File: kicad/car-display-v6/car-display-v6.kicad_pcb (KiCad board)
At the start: 4 copper layers, 35.8 x 35.8 mm, 38 parts, among them J1 AVR-ISP-10, J2 Screw_Terminal_01x03, J3 PicoBlade F 1x7, J4 Socket 1x6 0.1", J5 JMP 1x3 0.05", U1 ATmega328PB-M, U2 MCP25625T-E/ML, U3 TPSM365R1FRDNR, U4 TPSM365R15RDNR, Y1 16MHZ

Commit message: Work on V6 pCB
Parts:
- U3: value TPSM365R1FRDNR -> TPSM365R15FRDNR
- moved C17 0.13 mm to (96.5, 178.7)
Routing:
- net +12V: track 21.5 -> 4.43 mm, vias 0 -> 9
- net +3.3V: track 27.9 -> 30.2 mm
- net GND: vias 41 -> 49
- added copper zone on B.Cu, net +12V

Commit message: Work on V6 code for PlatformIO
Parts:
- removed the C1 at (91.2, 183.4)
- removed the C2 at (89.5, 182.8)
- removed the C3 at (83.4, 182.8)
- removed the C4 at (86.6, 177.8)
- added FB3: 120X, Inductor_SMD:L_0402_1005Metric, F.Cu at (91.2, 163.3)
- added FB4: 120X, Inductor_SMD:L_0402_1005Metric, F.Cu at (89.8, 163.3)
- added FB5: 120X, Inductor_SMD:L_0402_1005Metric, F.Cu at (88.4, 163.3)
- added FB6: 120X, Inductor_SMD:L_0402_1005Metric, F.Cu at (87.0, 163.3)
- added FB7: 120X, Inductor_SMD:L_0402_1005Metric, F.Cu at (85.6, 163.3)
- added H3: MountingHole_Pad, MountingHole:MountingHole_2.2mm_M2_DIN965, F.Cu at (84.5, 173.1)
- C1: renamed from C17; value C_Polarized -> 100uF
- FB1, FB2: value FerriteBead_Small_Array -> 120X; footprint jsdev:fb_array_0805 -> Inductor_SMD:L_0402_1005Metric
- U2: value MCP25625T-E/ML -> MCP2515-xST; footprint jsdev:QFN-28-1EP_6x6mm_P0.65mm_EP4.25x4.25mm_mod1 -> Package_SO:TSSOP-20_4.4x6.5mm_P0.65mm
- U3: value TPSM365R15FRDNR -> TCAN332; footprint jsdev:QFN-FCMOD_TI_11B -> jsdev:SOT-23-8-MOD
- moved H2 21.6 mm to (84.5, 187.1)
- moved U3 20.1 mm to (106.4, 178.6), turned to 0 degrees
- moved J4 16.2 mm to (115.6, 161.5), turned to 0 degrees
- moved J5 15.6 mm to (109.8, 173.0), turned to 180 degrees
- moved H1 15.2 mm to (114.9, 156.6)
- moved R4 14.8 mm to (111.9, 174.1), turned to 90 degrees
- moved R3 14.4 mm to (97.3, 172.7)
- moved C12 9.98 mm to (104.9, 167.4), turned to 180 degrees
- moved C3 9.78 mm to (91.2, 182.8)
- moved C4 9.78 mm to (89.5, 182.1)
- moved C5 9.78 mm to (83.4, 182.1)
- moved C6 9.78 mm to (86.6, 177.2)
- moved U4 9.78 mm to (86.6, 181.1)
- moved J1 9.09 mm to (87.2, 169.3)
- moved C2 8.30 mm to (111.0, 167.3), turned to -90 degrees
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- renumbered C13 to C10, C14 to C11, C15 to C12, C16 to C13, C9 to C2, C5 to C3, C6 to C4, C7 to C5, C8 to C6, C10 to C7, C11 to C8, C12 to C9, R6 to R1, R5 to R2, R8 to R3, R7 to R4
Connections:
- C13 pad 1: +5V -> +3.3V
- FB1 pad 2: /3F_SCK -> MOSI
- FB2 pad 1: /3F_CS_OLED -> /3F_SCK
- FB2 pad 2: /3F_GND -> SCK
- U1 pad 11: INT_CAN -> unconnected-(U1-PD7-Pad11)
- U1 pad 25: SEL_UNIT -> INT_CAN
- U1 pad 26: unconnected-(U1-PC3-Pad26) -> SEL_UNIT
- U2 pad 1: CS_CAN -> T_{X}CAN
- U2 pad 10: R_{X}CAN -> GND
- U2 pad 11: +3.3V -> unconnected-(U2-~{RX1BF}-Pad11)
- U2 pad 12: GND -> unconnected-(U2-~{RX0BF}-Pad12)
- U2 pad 13: CANH -> INT_CAN
- U2 pad 14: unconnected-(U2-NC-Pad14) -> SCK
- U2 pad 15: GND -> unconnected-(U2-NC-Pad15)
- U2 pad 16: T_{X}CAN -> MOSI
- U2 pad 17: unconnected-(U2-NC-Pad17) -> MISO
- U2 pad 18: GND -> CS_CAN
- U2 pad 19: +5V -> RESET
- U2 pad 2: RESET -> R_{X}CAN
- U2 pad 20: /CAN_CLK_PD -> +3.3V
- U2 pad 3: +3.3V -> unconnected-(U2-CLKOUT/SOF-Pad3)
- U2 pad 4: T_{X}CAN -> unconnected-(U2-~{TX0RTS}-Pad4)
- U2 pad 5: R_{X}CAN -> unconnected-(U2-~{TX1RTS}-Pad5)
- U2 pad 8: unconnected-(U2-~{TX1RTS}-Pad8) -> /CAN_CLK_PD
- U2 pad 9: unconnected-(U2-~{TX2RTS}-Pad9) -> CLK
- U3 pad 1: unconnected-(U3-PGOOD-Pad1) -> T_{X}CAN
- U3 pad 2: unconnected-(U3-EN-Pad2) -> GND
- U3 pad 3: +12V -> +3.3V
- U3 pad 4: +5V -> R_{X}CAN
- U3 pad 6: unconnected-(U3-SW-Pad6) -> GND
- U3 pad 7: unconnected-(U3-BOOT-Pad7) -> CANH
- U3 pad 8: Net-(U3-V_{CC}) -> unconnected-(U3-NC-Pad8)
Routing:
- net +5V: track 44.4 -> 0.00 mm, vias 6 -> 0
- net GND: track 38.7 -> 20.7 mm, vias 49 -> 46
- net R_{X}CAN: track 5.98 -> 17.1 mm
- net INT_CAN: track 11.6 -> 22.4 mm, vias 2 -> 0
- net MISO: track 23.8 -> 32.6 mm, vias 2 -> 3
- net FTDI_RX: track 9.42 -> 17.4 mm
- net CS_CAN: track 18.4 -> 10.6 mm, vias 2 -> 0
- net CLK: track 10.6 -> 18.3 mm
- net MOSI: track 33.9 -> 41.3 mm, vias 3 -> 4
- net RESET: track 37.2 -> 44.1 mm, vias 1 -> 2
- net SCK: track 36.1 -> 42.4 mm, vias 1 -> 4
- net /FTDI_RESET: track 17.8 -> 11.8 mm
- net FTDI_TX: track 11.1 -> 15.8 mm
- net CANH: track 16.8 -> 12.9 mm
- net +3.3V: track 30.2 -> 27.0 mm, vias 11 -> 12
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- removed copper zone on B.Cu, net +12V
- removed copper zone on B.Cu, net +3.3V
- removed copper zone on B.Cu, net +5V
- removed copper zone on F.Cu, net +5V
- removed copper zone on In2.Cu, net +5V
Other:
- board text added: "BATT"
- board text added: "FB1-7"
- board text added: "GMLAN-LS"
- board text added: "GND"
- board text added: "OLED CONNECTOR"

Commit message: Fix PSU error
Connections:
- C5 pad 1: Net-(U4-V_{CC}) -> Net-(U4-RT)
- U4 pad 11: +12V -> Net-(U4-RT)
- U4 pad 2: unconnected-(U4-EN-Pad2) -> +12V
- U4 pad 8: Net-(U4-V_{CC}) -> Net-(U4-RT)
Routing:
- net Net-(U4-RT): track 0.00 -> 7.78 mm, vias 0 -> 2
- net +12V: track 5.20 -> 2.17 mm
- net Net-(U4-V_{CC}): track 1.92 -> 0.00 mm

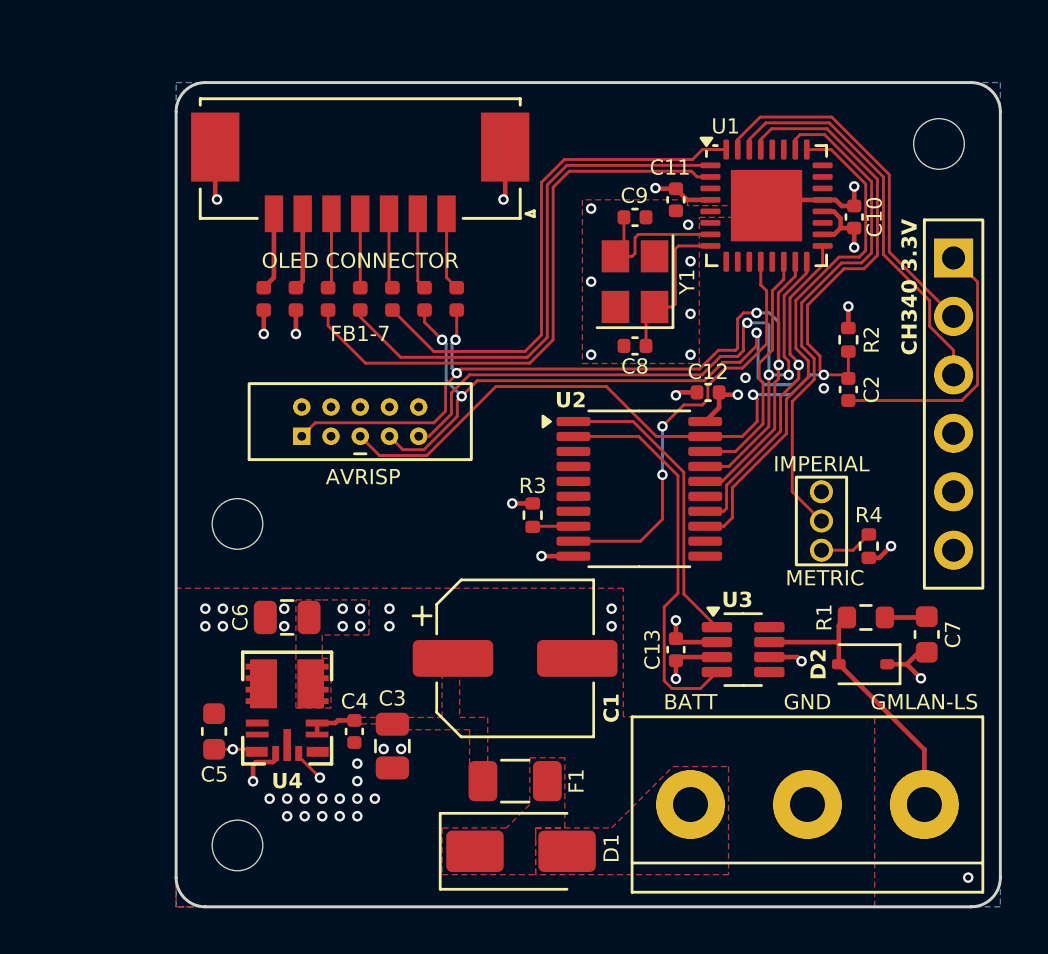
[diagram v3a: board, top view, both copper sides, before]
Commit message: Update PCB with new power supply and return to MCP25625
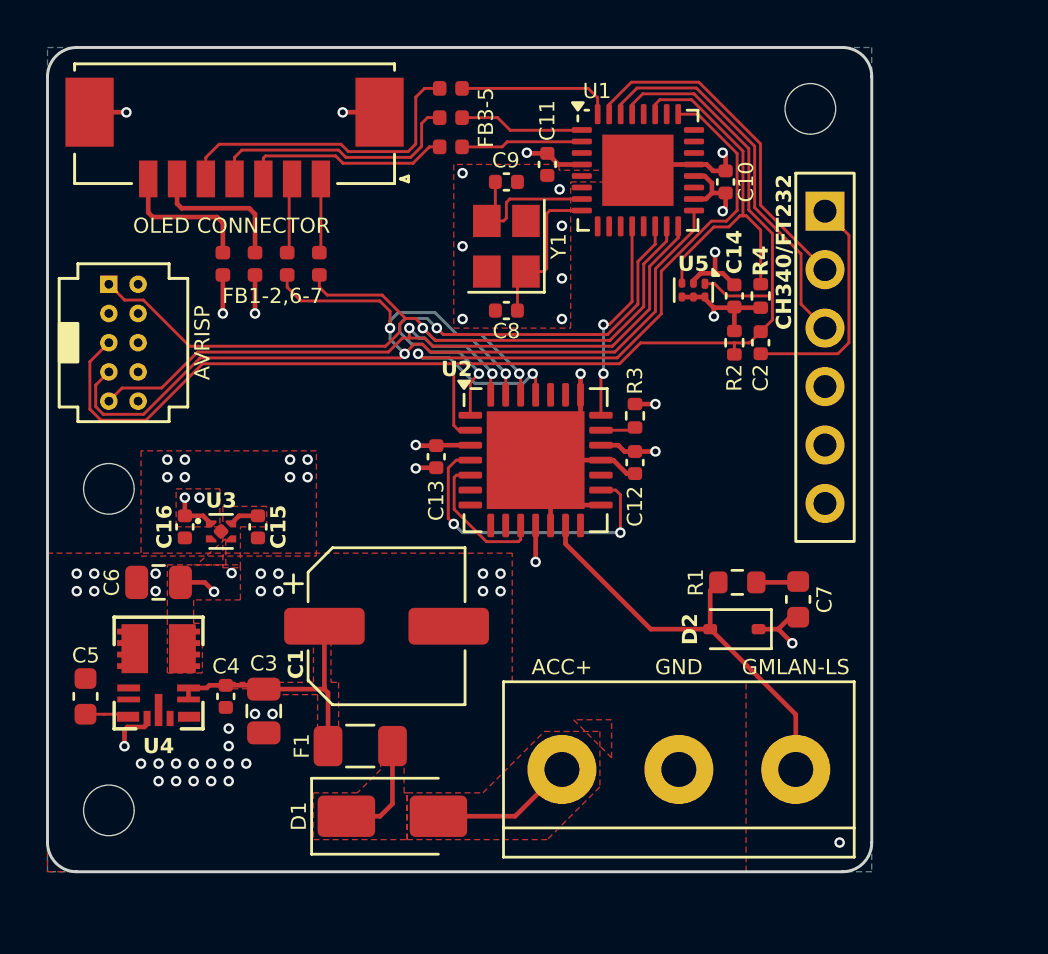
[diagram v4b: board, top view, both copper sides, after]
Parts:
- removed J5: JMP 1x3 0.05", jsdev:PinHeader_1x03_P1.27mm_Vertical_mod
- added C14: 100nF, Capacitor_SMD:C_0402_1005Metric, F.Cu at (106.0, 163.2)
- added C15: 100nF, Capacitor_SMD:C_0402_1005Metric, F.Cu at (85.3, 173.2)
- added C16: 100nF, Capacitor_SMD:C_0402_1005Metric, F.Cu at (82.2, 173.2)
- added U5: TPS3422, Package_SON:Texas_USON-6_1x1.45mm_P0.5mm_SMD, F.Cu at (104.3, 162.9)
- J1: footprint jsdev:PinHeader_ISP10_POGO -> jsdev:PinHeader_SWD_BD120-10-A-0305-0229-L-B
- U2: value MCP2515-xST -> MCP25625T-E/ML; footprint Package_SO:TSSOP-20_4.4x6.5mm_P0.65mm -> Package_DFN_QFN:QFN-28-1EP_6x6mm_P0.65mm_EP4.25x4.25mm
- U3: value TCAN332 -> 3.3V; footprint jsdev:SOT-23-8-MOD -> jsdev:Texas_X2SON-4_1x1mm_P0.65mm_MOD
- U4: value TPSM365R15RDNR -> TPSM365R15FRDNR
- moved U3 23.3 mm to (83.7, 173.4)
- moved C13 13.4 mm to (93.1, 170.2), turned to -90 degrees
- moved R4 11.8 mm to (107.2, 163.2), turned to -90 degrees
- moved FB7 10.6 mm to (93.7, 154.2), turned to 0 degrees
- moved J3 10.0 mm to (84.3, 155.7)
- moved FB6 8.80 mm to (93.7, 155.4), turned to 0 degrees
- moved J1 8.75 mm to (79.5, 165.2), turned to 0 degrees
- moved FB5 7.08 mm to (93.7, 156.7), turned to 0 degrees
- moved F1 6.90 mm to (89.8, 182.8)
- moved R3 6.20 mm to (101.7, 168.4)
- moved FB4 6.16 mm to (88.0, 161.8)
- moved FB3 6.16 mm to (86.6, 161.8)
- moved J4 5.95 mm to (110.0, 159.5)
- moved C9 5.80 mm to (96.1, 158.2)
- moved Y1 5.80 mm to (96.1, 161.0)
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- renumbered FB7 to FB1, FB6 to FB2, FB2 to FB3, FB1 to FB4, FB3 to FB5, FB4 to FB6, FB5 to FB7
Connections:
- C12 pad 1: +3.3V -> +5V
- C5 pad 1: Net-(U4-RT) -> Net-(U4-V_{CC})
- C6 pad 1: +3.3V -> +5V
- J4 pad 4: +3.3V -> unconnected-(J4-Pin_4-Pad4)
- R3 pad 1: /CAN_CLK_PD -> Net-(U2-OSC2)
- R4 pad 1: +3.3V -> SW_RESET
- R4 pad 2: /SEL_METRIC -> +3.3V
- U1 pad 13: unconnected-(U1-PB1-Pad13) -> UNIT_SENSE
- U1 pad 2: CS_OLED -> DC_OLED
- U1 pad 27: unconnected-(U1-PC4-Pad27) -> SW_RESET
- U1 pad 32: DC_OLED -> CS_OLED
- U2 pad 1: T_{X}CAN -> CS_CAN
- U2 pad 10: GND -> Net-(U2-R_{XD})
- U2 pad 11: unconnected-(U2-~{RX1BF}-Pad11) -> +3.3V
- U2 pad 12: unconnected-(U2-~{RX0BF}-Pad12) -> GND
- U2 pad 13: INT_CAN -> CANH
- U2 pad 14: SCK -> unconnected-(U2-NC-Pad14)
- U2 pad 15: unconnected-(U2-NC-Pad15) -> GND
- U2 pad 16: MOSI -> Net-(U2-T_{XD})
- U2 pad 17: MISO -> unconnected-(U2-NC-Pad17)
- U2 pad 18: CS_CAN -> GND
- U2 pad 19: RESET -> +5V
- U2 pad 2: R_{X}CAN -> RESET
- U2 pad 20: +3.3V -> Net-(U2-OSC2)
- U2 pad 3: unconnected-(U2-CLKOUT/SOF-Pad3) -> +3.3V
- U2 pad 4: unconnected-(U2-~{TX0RTS}-Pad4) -> Net-(U2-T_{XD})
- U2 pad 5: unconnected-(U2-~{TX1RTS}-Pad5) -> Net-(U2-R_{XD})
- U2 pad 8: /CAN_CLK_PD -> unconnected-(U2-~{TX1RTS}-Pad8)
- U2 pad 9: CLK -> unconnected-(U2-~{TX2RTS}-Pad9)
- U3 pad 1: T_{X}CAN -> +3.3V
- U3 pad 3: +3.3V -> +5V
- U3 pad 4: R_{X}CAN -> +5V
- U3 pad 5: unconnected-(U3-NC-Pad5) -> GND
- U4 pad 11: Net-(U4-RT) -> GND
- U4 pad 4: +3.3V -> +5V
- U4 pad 8: Net-(U4-RT) -> Net-(U4-V_{CC})
- U4 pad 9: +3.3V -> +5V
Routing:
- net +5V: track 0.00 -> 38.3 mm, vias 0 -> 4
- net SEL_UNIT: track 22.3 -> 0.00 mm
- net CS_OLED: track 25.4 -> 6.77 mm
- net RST_OLED: track 23.6 -> 5.44 mm
- net DC_OLED: track 22.8 -> 5.30 mm
- net R_{X}CAN: track 17.1 -> 0.00 mm
- net SW_RESET: track 0.00 -> 15.9 mm
- net Net-(U2-T_{XD}): track 0.00 -> 13.6 mm, vias 0 -> 2
- net T_{X}CAN: track 13.0 -> 0.00 mm
- net GND: track 20.7 -> 33.5 mm, vias 46 -> 55
- net RESET: track 44.1 -> 56.6 mm, vias 2 -> 0
- net CS_CAN: track 10.6 -> 21.5 mm, vias 0 -> 2
- net /3F_CS_OLED: track 3.27 -> 13.8 mm
- net +12V: track 2.17 -> 11.8 mm
- net CLK: track 18.3 -> 8.90 mm
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- added copper zone on F.Cu, net +5V
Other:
- board text added: "ACC+"
- board text added: "CH340/FT232"
- board text added: "FB1-2,6-7"
- board text added: "FB3-5"
- board text removed: "BATT"
- board text removed: "CH340 3.3V"
- board text removed: "FB1-7"
- board text removed: "IMPERIAL"
- board text removed: "METRIC"
